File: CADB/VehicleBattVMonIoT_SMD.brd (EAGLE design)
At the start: 68 x 50 mm, 62 parts, among them IC1 24AA02E64, J1 CON_HEADER_1X06-SMD-RIGHT-ANG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, M1 ARDUINO-PRO-MINI-3.3V#APC, U1 DC-DC-STEP-DOWN-MP1584, U3 RFM69HCW, U4 SPI_FLASH-X25XXSMD, X1 BU-SMA-G

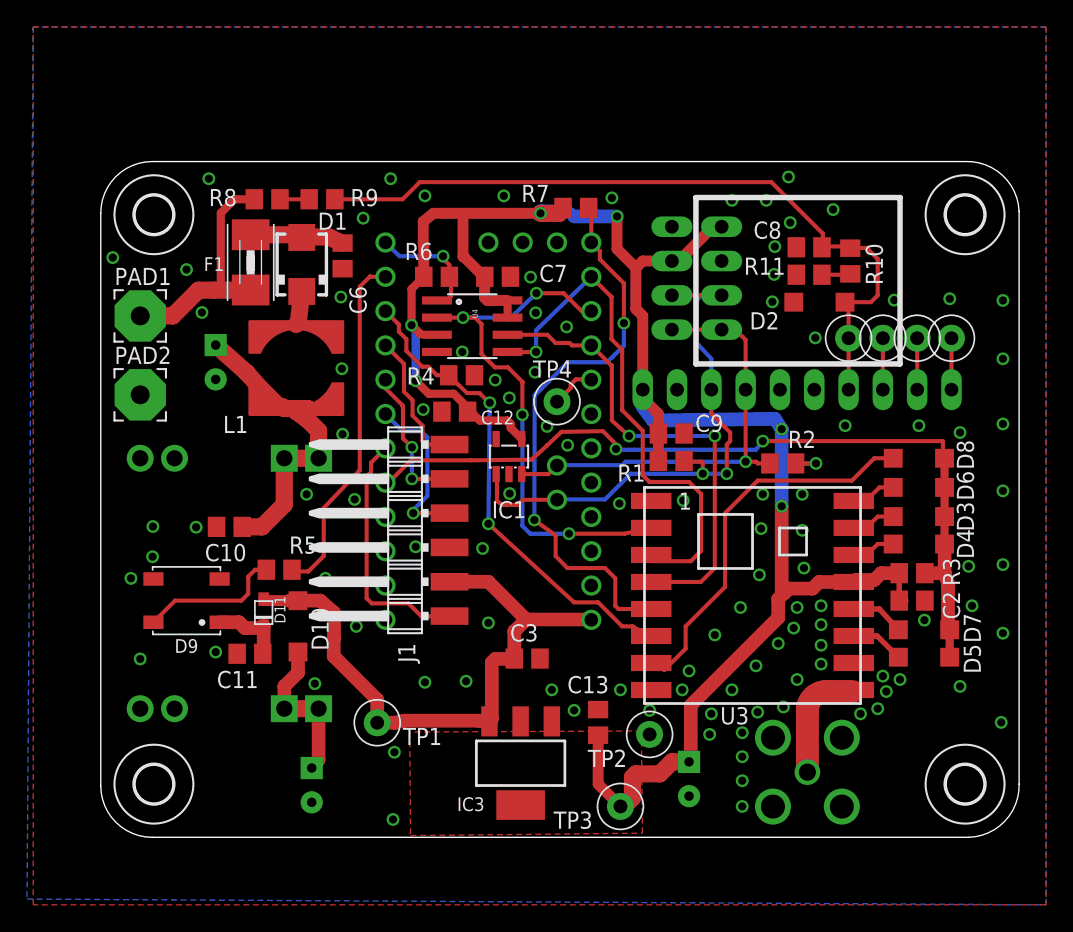
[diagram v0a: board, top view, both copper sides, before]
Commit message: Latest CAD B and re-arrange structure
seperate directory for CADA CADB.
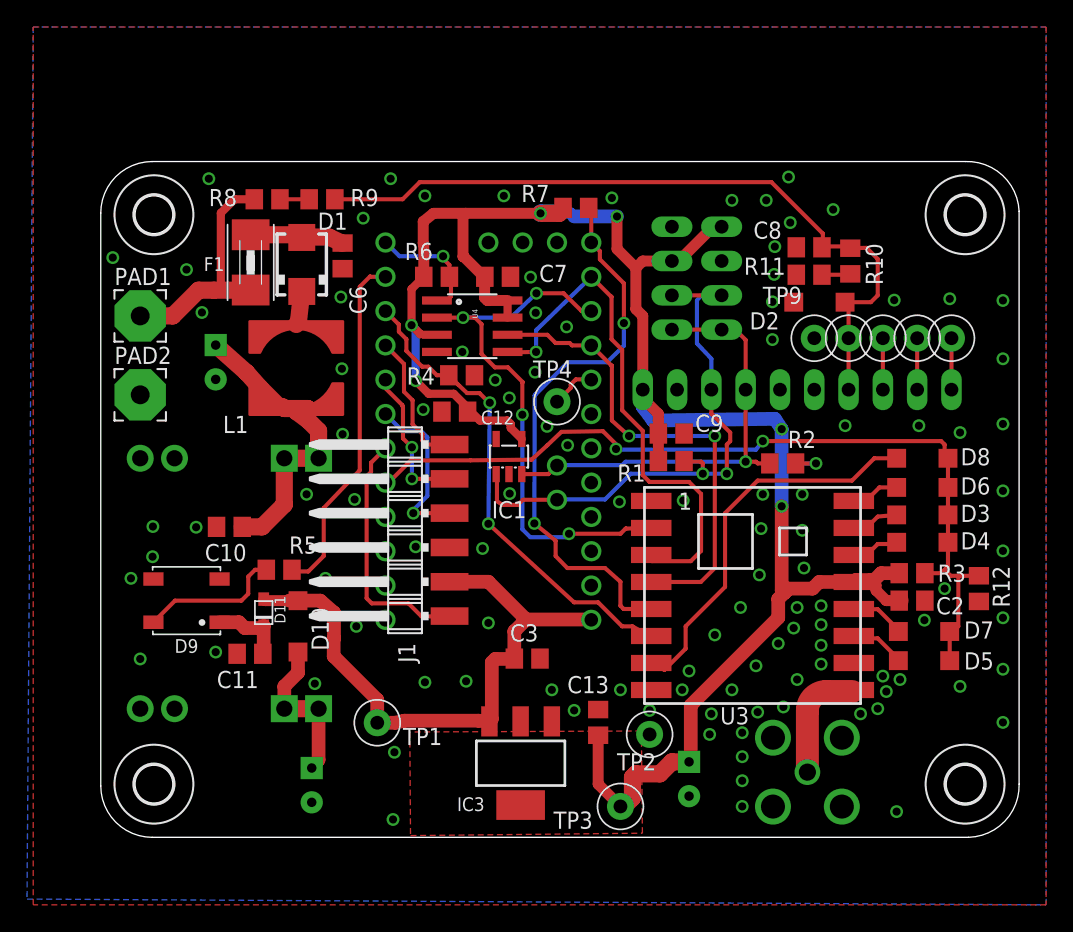
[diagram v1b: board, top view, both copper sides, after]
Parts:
- added R12: 10k, 5%, rcl:R0805
- added TP9: TP_1MM_TH", TP_1MM_TH:TP_1MM_TH
- C1, C4, C5: value 100uF, 25V -> 100uF, 25V, 85C
- C10, C11, C13, C2, C3, C7, C9: value 1uF, 0805, 25V -> 1uF, 0805, 25V, X5R
- C12: value 1u, 0805, 25v -> 1uF, 0805, 25V, X5R
- C6: value 1u, 0805, 25V -> 1uF, 0805, 25V, X5R
- C8: value 1n, 0805, 16v -> 1NF, 0805, 16V, X5R
- D5, D7, D8: value MBR0520LT -> NOFIT
- D9: value (none) -> WS2812B
- IC3: value (none) -> LM1117
- J1: value CON_HEADER_1X06-SMD-RIGHT-ANGLED -> HM-10 MODULE
- JP1: value (none) -> SHT31 MODULE
- JP2: value (none) -> OLED MODULE
- R1, R2, R6, R7: value 10k -> 10k, 5%
- R10, R11: value (none) -> 22k, 1%
- R3: value 4k7 -> NOFIT
- R4: value 10k -> NOFIT
- R5: value 1k -> 1k, 5%
- R8, R9: value (none) -> 100k, 1%
- SV1: value (none) -> ADS1115 MODULE
- U3: value RFM69HCW -> RFM9xW
- U4: value SPI_FLASH-X25XXSMD -> W25Q80DVSNIG
- moved D3 0.28 mm to (60.8, 23.9), turned to 180 degrees
- moved D4 0.28 mm to (60.8, 21.8), turned to 180 degrees
- moved D5 0.25 mm to (61.0, 13.1), turned to 180 degrees
- moved D6 0.25 mm to (60.8, 25.9), turned to 180 degrees
- moved D8 0.25 mm to (60.8, 28.1), turned to 180 degrees
- moved D7 0.13 mm to (61.0, 15.2), turned to 180 degrees
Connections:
- net /INT: now also D3.C, D4.C, D5.C, D6.C, D7.C, D8.C, R12.2; no longer D3.A, D4.A, D5.A, D6.A, D7.A, D8.A
- net DIO0: now also D4.A; no longer D4.C
- net DIO1: now also D3.A; no longer D3.C
- net DIO2: now also D6.A; no longer D6.C
- net DIO3: now also D5.A; no longer D5.C
- net DIO4: now also D7.A; no longer D7.C
- net DIO5: now also D8.A; no longer D8.C
- net GND: now also R12.1, TP9.P$1
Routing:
- net /INT: track 63.9 -> 65.3 mm
- net +3V3: track 148.1 -> 149.0 mm
- net GND: vias 105 -> 106

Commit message: minor updates
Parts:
- removed IC1: 24AA02E64, microchip:SOT23-5L
- added U2: MICROCHIP-24AA02E64T_24AA02E64T-I/OT, WeMos-Lora:MICROCHIP-24AA02E64T_SOT95P270X145-5N
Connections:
- net +3V3: now also U2.4; no longer IC1.4
- net GND: now also U2.2; no longer IC1.2
- net SCL: now also U2.1; no longer IC1.1
- net SDA: now also U2.3; no longer IC1.3
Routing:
- net GND: track 0.19 -> 4.17 mm
